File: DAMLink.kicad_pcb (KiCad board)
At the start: 2 copper layers, 41 x 33 mm, 71 parts, among them J1 USB_C_Receptacle_Host, J3 ARM_JTAG_SWD_10_Male, J4 VCCIO_EXT, J5 PicoBlade, P1 USB_C_Plug, SW1 SW_DIP_x04, U1 FT230XQ, U2 PI5A3157CEX, U3 PI5A3157CEX, U4 USB3740B-AI2, U5 SiP32432DR3

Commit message: Add new footprint
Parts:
- removed C6: 100nF, Capacitor_SMD:C_0603_1608Metric
- removed R15: 680R, Resistor_SMD:R_0603_1608Metric
- removed SWD1: TC2030, Connector:Tag-Connect_TC2030-IDC-FP_2x03_P1.27mm_Vertical
- removed TP18: TestPoint_Small, tuna-f1sh/jbr-kicad/Misc.pretty:TestPoint_Pad_D1.0mm_Tight
- added C3: 100nF, Capacitor_SMD:C_0603_1608Metric, F.Cu at (116.5, 45.5)
- added C5: 100nF, Capacitor_SMD:C_0603_1608Metric, F.Cu at (116.5, 48.0)
- added D1: TXD, LED_SMD:LED_0603_1608Metric, F.Cu at (135.9, 45.5)
- added D2: RXD, LED_SMD:LED_0603_1608Metric, F.Cu at (135.9, 48.1)
- added J1: PicoBlade, Connector_Molex:Molex_PicoBlade_53048-0610_1x06_P1.25mm_Horizontal, F.Cu at (155.9, 76.3)
- added J3: PicoBlade, Connector_PinHeader_1.27mm:PinHeader_1x04_P1.27mm_Vertical, F.Cu at (137.0, 54.6)
- added J6: Conn_ST_STDC14, Connector_STDC14:SAMTEC_FTSH-107-01-L-DV-K-A, F.Cu at (171.5, 66.5)
- added JP1: SolderJumper_2_Bridged, Jumper:SolderJumper-2_P1.3mm_Bridged_RoundedPad1.0x1.5mm, F.Cu at (112.3, 46.0)
- added JP5: SolderJumper_3_Bridged12, Jumper:SolderJumper-3_P1.3mm_Bridged12_RoundedPad1.0x1.5mm, F.Cu at (125.7, 67.8)
- added JP6: SolderJumper_2_Bridged, Jumper:SolderJumper-2_P1.3mm_Bridged_RoundedPad1.0x1.5mm, F.Cu at (112.3, 49.6)
- added JP7: SolderJumper_2_Bridged, Jumper:SolderJumper-2_P1.3mm_Bridged_RoundedPad1.0x1.5mm, F.Cu at (112.3, 53.1)
- added JP8: SolderJumper_2_Bridged, Jumper:SolderJumper-2_P1.3mm_Bridged_RoundedPad1.0x1.5mm, F.Cu at (112.3, 56.7)
- added JP9: SolderJumper_2_Bridged, Jumper:SolderJumper-2_P1.3mm_Bridged_RoundedPad1.0x1.5mm, F.Cu at (112.3, 60.2)
- added R10: 680R, Resistor_SMD:R_0603_1608Metric, F.Cu at (120.5, 55.5)
- added R3: 22k, Resistor_SMD:R_0603_1608Metric, F.Cu at (116.5, 50.5)
- added R4: 22k, Resistor_SMD:R_0603_1608Metric, F.Cu at (116.5, 53.0)
- added R5: 1k, Resistor_SMD:R_0603_1608Metric, F.Cu at (116.5, 55.5)
- added R6: 1k, Resistor_SMD:R_0603_1608Metric, F.Cu at (120.5, 45.5)
- added R7: 680R, Resistor_SMD:R_0603_1608Metric, F.Cu at (120.5, 48.0)
- added R8: 680R, Resistor_SMD:R_0603_1608Metric, F.Cu at (120.5, 50.5)
- added R9: 680R, Resistor_SMD:R_0603_1608Metric, F.Cu at (120.5, 53.0)
- added TP1: TestPoint_Small, TestPoint:TestPoint_Pad_D1.0mm, F.Cu at (201.0, 39.9)
- added TP10: TestPoint_Small, TestPoint:TestPoint_Pad_D1.0mm, F.Cu at (201.0, 49.0)
- added TP2: TestPoint_Small, TestPoint:TestPoint_Pad_D1.0mm, F.Cu at (201.0, 42.9)
- added TP9: TestPoint_Small, TestPoint:TestPoint_Pad_D1.0mm, F.Cu at (201.0, 46.0)
- added U2: USB3740B-AI2, Package_DFN_QFN:UQFN-10_1.3x1.8mm_P0.4mm, F.Cu at (136.2, 70.3)
- added U3: TMUX1574RSVR, TMUX1574RSVR:IC_TMUX1574RSVR, F.Cu at (139.2, 78.8)
- added U4: USBLC6-4SC6, Package_TO_SOT_SMD:SOT-23-6, F.Cu at (134.4, 37.2)
- added U6: USBLC6-4SC6, Package_TO_SOT_SMD:SOT-23-6, F.Cu at (134.4, 41.9)
- C1: value 100nF -> 10nF
- J3: value ARM_JTAG_SWD_10_Male -> PicoBlade; footprint tuna-f1sh/jbr-kicad/Misc.pretty:20021521-00010T1LF -> Connector_PinHeader_1.27mm:PinHeader_1x04_P1.27mm_Vertical
- J5: value PicoBlade -> TC2050-IDC; footprint Connector_PinHeader_1.27mm:PinHeader_1x04_P1.27mm_Vertical -> TC2050-IDC:TAG-CONNECT_TC2050-IDC
- JP2: value SolderJumper_2_Bridged -> SolderJumper_3_Bridged12; footprint Jumper:SolderJumper-2_P1.3mm_Bridged_RoundedPad1.0x1.5mm -> Jumper:SolderJumper-3_P1.3mm_Bridged12_RoundedPad1.0x1.5mm
- R1, R2: value 1k -> 5k1
- R5, R6: value 22k -> 1k
- TP11, TP12, TP13, TP14, TP15, TP16, TP17, TP3, TP4, TP5, TP6, TP7, TP8: footprint tuna-f1sh/jbr-kicad/Misc.pretty:TestPoint_Pad_D1.0mm_Tight -> TestPoint:TestPoint_Pad_D1.0mm
- TP13: renamed from TP9; footprint tuna-f1sh/jbr-kicad/Misc.pretty:TestPoint_Pad_D1.0mm_Tight -> TestPoint:TestPoint_Pad_D1.0mm
- TP14: renamed from TP2; footprint tuna-f1sh/jbr-kicad/Misc.pretty:TestPoint_Pad_D1.0mm_Tight -> TestPoint:TestPoint_Pad_D1.0mm
- TP15: renamed from TP19; footprint tuna-f1sh/jbr-kicad/Misc.pretty:TestPoint_Pad_D1.0mm_Tight -> TestPoint:TestPoint_Pad_D1.0mm
- TP16: renamed from TP10; footprint tuna-f1sh/jbr-kicad/Misc.pretty:TestPoint_Pad_D1.0mm_Tight -> TestPoint:TestPoint_Pad_D1.0mm
- TP17: renamed from TP1; footprint tuna-f1sh/jbr-kicad/Misc.pretty:TestPoint_Pad_D1.0mm_Tight -> TestPoint:TestPoint_Pad_D1.0mm
- U2: value PI5A3157CEX -> USB3740B-AI2; footprint Package_TO_SOT_SMD:SOT-363_SC-70-6 -> Package_DFN_QFN:UQFN-10_1.3x1.8mm_P0.4mm
- U3: value PI5A3157CEX -> TMUX1574RSVR; footprint Package_TO_SOT_SMD:SOT-363_SC-70-6 -> TMUX1574RSVR:IC_TMUX1574RSVR
- U4: value USB3740B-AI2 -> USBLC6-4SC6; footprint Package_DFN_QFN:UQFN-10_1.3x1.8mm_P0.4mm -> Package_TO_SOT_SMD:SOT-23-6
- moved G*** 50.6 mm to (214.1, 64.6)
- moved J5 33.4 mm to (181.5, 60.5), turned to 180 degrees
- moved J3 26.2 mm to (155.6, 39.5), turned to 90 degrees
- moved U3 1.30 mm to (173.0, 54.5)
- moved TP4 0.75 mm to (168.0, 50.5)
- renumbered C2 to C1, C3 to C2, D4 to D3, J1 to J2, JP5 to JP2, JP6 to JP3, R12 to R1, R14 to R11, R16 to R12, R10 to R13, R11 to R14, R13 to R2
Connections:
- C1 pad 1: +3V3 -> Net-(C1-Pad1)
- C1 pad 1: Net-(C2-Pad1) -> Net-(C1-Pad1)
- FB1 pad 1: Net-(C2-Pad1) -> Net-(C1-Pad1)
- J2 pad A4: Net-(C2-Pad1) -> Net-(C1-Pad1)
- J2 pad A9: Net-(C2-Pad1) -> Net-(C1-Pad1)
- J2 pad B4: Net-(C2-Pad1) -> Net-(C1-Pad1)
- J2 pad B9: Net-(C2-Pad1) -> Net-(C1-Pad1)
- J3 pad 1: /VREF -> VCC
- J3 pad 2: /SWDIO -> /DEV_TXD
- J3 pad 3: GND -> /DEV_RXD
- J3 pad 4: /SWCLK -> GND
- J5 pad 1: VCC -> /VREF
- J5 pad 2: /DEV_TXD -> /SWDIO
- J5 pad 3: /DEV_RXD -> GND
- J5 pad 4: GND -> /SWCLK
- JP1 pad 1: /DEV_RXD -> Net-(JP1-A)
- JP1 pad 2: Net-(JP1-B) -> VBUS
- JP2 pad 3: Net-(JP5-B) -> Net-(JP2-B)
- JP2 pad 1: /DEV_TXD -> /VTARGET
- JP2 pad 2: Net-(JP2-B) -> VCC
- JP3 pad 1: /VTARGET -> +3V3
- JP3 pad 2: /VREF -> Net-(JP2-B)
- JP3 pad 3: VCC -> Net-(J4-Pin_1)
- JP3 pad 2: Net-(JP5-B) -> Net-(JP2-B)
- JP7 pad 1: Net-(JP7-A) -> /DEV_TXD
- JP7 pad 2: VBUS -> Net-(J6-VCP_TX)
- P1 pad A2: /SWDIO -> /DEV_TX+
- P1 pad A3: /SWCLK -> /DEV_TX-
- P1 pad B2: /SWDIO -> /DEV_TX+
- P1 pad B3: /SWCLK -> /DEV_TX-
- R1 pad 1: Net-(D1-K) -> /HOST_CC2
- R1 pad 2: /TXLED/CB1 -> GND
- R2 pad 1: Net-(D2-K) -> /HOST_CC1
- R2 pad 2: /RXLED/CB2 -> GND
- R3 pad 1: /UART_USB -> /~{PASS_USB}
- R4 pad 1: /~{PASS_USB} -> /UART_USB
- R5 pad 1: /SWT_RX+ -> Net-(D1-K)
- R5 pad 2: GND -> /TXLED/CB1
- R6 pad 1: /SWT_RX- -> Net-(D2-K)
- R6 pad 2: GND -> /RXLED/CB2
- TP11 pad 1: /HOST_D+ -> /DEV_D+
- TP12 pad 1: /HOST_D- -> /DEV_D-
- TP13 pad 1: /UART_D+ -> /SWDIO
- TP14 pad 1: /UART_D- -> /SWCLK
- TP15 pad 1: /DEV_D+ -> /VREF
- TP16 pad 1: /DEV_D- -> /~{RESET}
- TP17 pad 1: /DEV_RX+ -> /SWO
- TP3 pad 1: /TXDEN/CB0 -> /~{PASS_USB}
- TP4 pad 1: /TXLED/CB1 -> /UART_USB
- TP5 pad 1: /RXLED/CB2 -> /TXDEN/CB0
- TP6 pad 1: /SLEEP/CB3 -> /TXLED/CB1
- TP7 pad 1: /~{PASS_USB} -> /RXLED/CB2
- TP8 pad 1: /UART_USB -> /SLEEP/CB3
- U1 pad 10: Net-(JP7-A) -> Net-(JP1-A)
- U1 pad 15: /DEV_TXD -> Net-(JP8-A)
- U1 pad 2: /DEV_RXD -> Net-(JP9-A)
- U2 pad 1: Net-(JP1-B) -> /DEV_D-
- U2 pad 2: GND -> /DEV_D+
- U2 pad 3: /~{RESET} -> /~{PASS_USB}
- U2 pad 4: /DEV_RX- -> /UART_USB
- U2 pad 5: VCC -> VBUS
- U2 pad 6: /SWT_RX- -> /UART_D+
- U3 pad 1: Net-(JP2-B) -> /IO0
- U3 pad 2: GND -> /DEV_TX-
- U3 pad 3: /SWO -> /SWDIO
- U3 pad 4: /DEV_RX+ -> /IO1
- U3 pad 5: VCC -> /DEV_TX+
- U3 pad 6: /SWT_RX+ -> GND
- U4 pad 1: /DEV_D- -> /DEV_RX-
- U4 pad 2: /DEV_D+ -> GND
- U4 pad 3: /~{PASS_USB} -> /DEV_RX+
- U4 pad 4: /UART_USB -> /VTARGET
- U4 pad 6: /UART_D+ -> /VTARGET
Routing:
- net /~{RESET}: track 59.6 -> 0.00 mm, vias 5 -> 0
- net VCC: track 87.4 -> 34.9 mm, vias 6 -> 1
- net /SWT_RX+: track 51.7 -> 0.00 mm, vias 6 -> 0
- net /RXLED/CB2: track 46.5 -> 0.00 mm, vias 3 -> 0
- net /SWCLK: track 44.3 -> 0.00 mm, vias 4 -> 0
- net /SWDIO: track 44.0 -> 0.00 mm, vias 4 -> 0
- net /DEV_D-: track 29.4 -> 0.00 mm, vias 2 -> 0
- net /SWO: track 28.1 -> 0.00 mm, vias 4 -> 0
- net /DEV_D+: track 28.1 -> 0.00 mm, vias 2 -> 0
- net GND: track 58.8 -> 31.8 mm, vias 5 -> 4
- net /~{DEV_ON}: track 26.0 -> 1.54 mm, vias 4 -> 0
- net /VTARGET: track 38.1 -> 13.7 mm, vias 6 -> 2
- net /UART_USB: track 22.6 -> 0.00 mm, vias 3 -> 0
- net /DEV_RX+: track 33.4 -> 12.2 mm, vias 3 -> 0
- net /DEV_RX-: track 29.8 -> 8.98 mm, vias 3 -> 0
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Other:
- board text added: "DAMLink R${REVISION}"
- board text removed: "Minnow R${REVISION}"

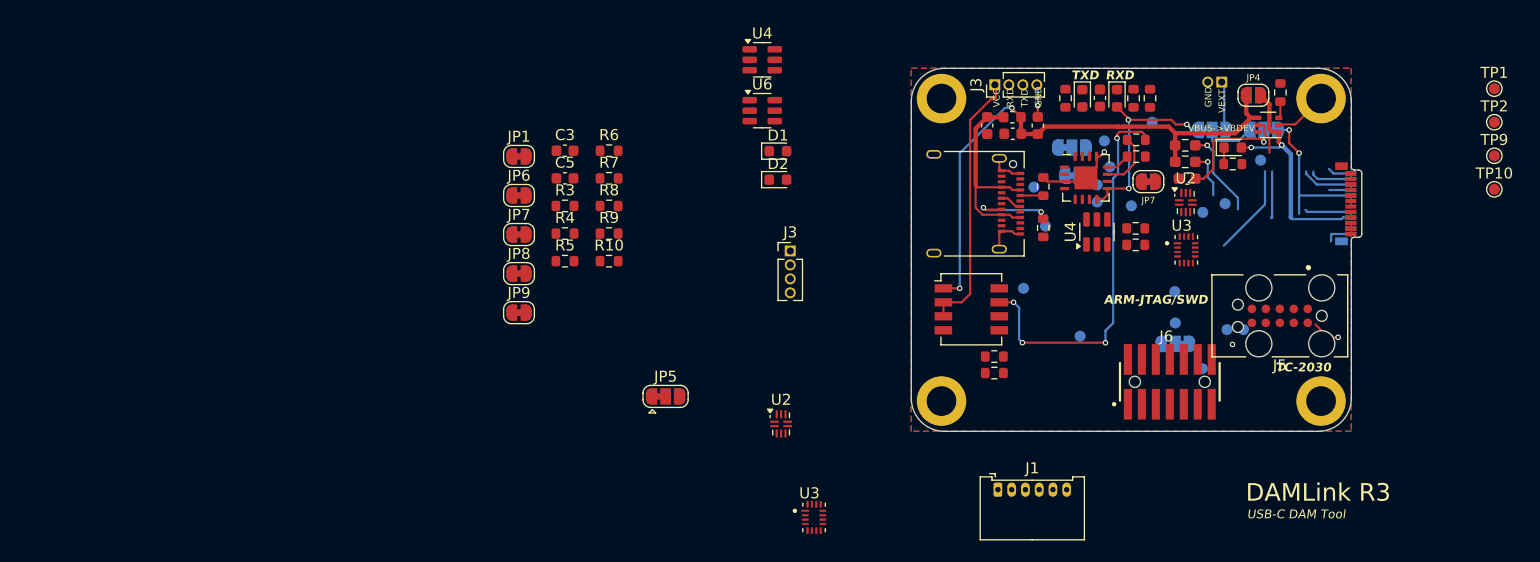
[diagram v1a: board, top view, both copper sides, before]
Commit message: Remove wrong libraries
Remove "altium" libraries which where downloaded wrong from SnapEDA.

Import correct libraries from Manufracturer and from UltranLibrary

Clear whole PCB.
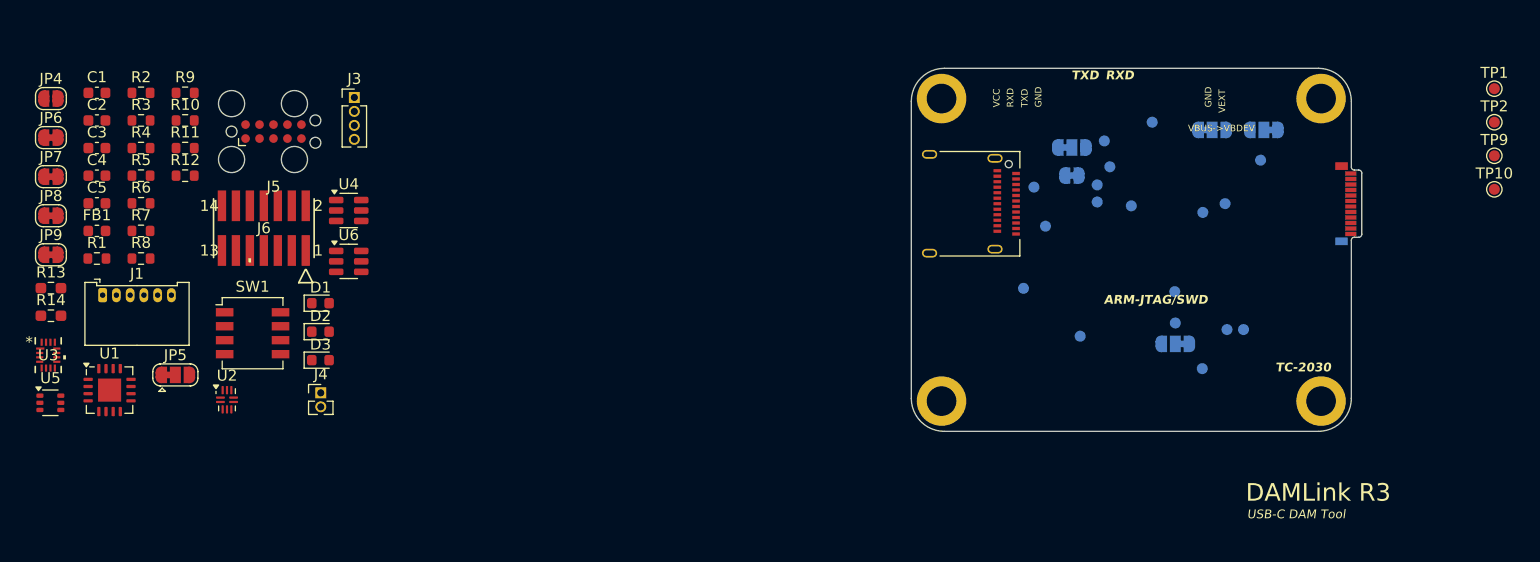
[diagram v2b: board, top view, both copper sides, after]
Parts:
- removed the C1 at (165.2, 40.7)
- removed the C1 at (154.9, 43.2)
- removed the C5 at (173.1, 48.0)
- removed the C5 at (116.5, 48.0)
- removed the D1 at (135.9, 45.5)
- removed the D1 at (163.6, 40.7)
- removed the D2 at (166.7, 40.7)
- removed the D2 at (135.9, 48.1)
- removed the J3 at (137.0, 54.6)
- removed the J3 at (155.6, 39.5)
- removed the JP1 at (112.3, 46.0)
- removed the JP7 at (112.3, 53.1)
- removed the JP7 at (169.6, 48.3)
- removed the R1 at (160.0, 52.5)
- removed the R1 at (162.0, 40.7)
- removed the R2 at (168.2, 40.7)
- removed the R2 at (160.0, 48.8)
- removed the R3 at (116.5, 50.5)
- removed the R3 at (168.4, 52.5)
- removed the R4 at (116.5, 53.0)
- removed the R4 at (168.4, 54.0)
- removed the R5 at (116.5, 55.5)
- removed the R5 at (155.6, 65.7)
- removed the R6 at (120.5, 45.5)
- removed the R6 at (155.6, 64.2)
- removed the R7 at (120.5, 48.0)
- removed the R7 at (168.4, 46.0)
- removed the R8 at (120.5, 50.5)
- removed the R8 at (168.4, 44.5)
- removed the R9 at (169.7, 40.7)
- removed the R9 at (120.5, 53.0)
- removed the U2 at (136.2, 70.3)
- removed the U2 at (172.9, 50.2)
- removed the U3 at (139.2, 78.8)
- removed the U3 at (173.0, 54.5)
- removed the U4 at (134.4, 37.2)
- removed the U4 at (164.9, 52.9)
- added C1: 10nF, Capacitor_SMD:C_0603_1608Metric, F.Cu at (74.0, 40.2)
- added C5: 100nF, Capacitor_SMD:C_0603_1608Metric, F.Cu at (74.0, 50.3)
- added D1: TXD, LED_SMD:LED_0603_1608Metric, F.Cu at (94.3, 59.4)
- added D2: RXD, LED_SMD:LED_0603_1608Metric, F.Cu at (94.3, 61.9)
- added J3: PicoBlade, Connector_PinHeader_1.27mm:PinHeader_1x04_P1.27mm_Vertical, F.Cu at (97.4, 40.6)
- added JP7: SolderJumper_2_Bridged, Jumper:SolderJumper-2_P1.3mm_Bridged_RoundedPad1.0x1.5mm, F.Cu at (69.8, 47.9)
- added R1: 5k1, Resistor_SMD:R_0603_1608Metric, F.Cu at (74.0, 55.3)
- added R2: 5k1, Resistor_SMD:R_0603_1608Metric, F.Cu at (78.0, 40.2)
- added R3: 22k, Resistor_SMD:R_0603_1608Metric, F.Cu at (78.0, 42.7)
- added R4: 22k, Resistor_SMD:R_0603_1608Metric, F.Cu at (78.0, 45.2)
- added R5: 1k, Resistor_SMD:R_0603_1608Metric, F.Cu at (78.0, 47.8)
- added R6: 1k, Resistor_SMD:R_0603_1608Metric, F.Cu at (78.0, 50.3)
- added R7: 680R, Resistor_SMD:R_0603_1608Metric, F.Cu at (78.0, 52.8)
- added R8: 680R, Resistor_SMD:R_0603_1608Metric, F.Cu at (78.0, 55.3)
- added R9: 680R, Resistor_SMD:R_0603_1608Metric, F.Cu at (82.0, 40.2)
- added U2: USB3740B-AI2, Package_DFN_QFN:UQFN-10_1.3x1.8mm_P0.4mm, F.Cu at (85.8, 68.1)
- added U3: TMUX1574RSVR, TMUX1574RSVR:RSV16_TEX, F.Cu at (69.5, 64.1)
- added U4: USBLC6-4SC6, Package_TO_SOT_SMD:SOT-23-6, F.Cu at (96.9, 50.9)
- J5: footprint TC2050-IDC:TAG-CONNECT_TC2050-IDC -> Connector:Tag-Connect_TC2050-IDC-FP_2x05_P1.27mm_Vertical
- J6: footprint Connector_STDC14:SAMTEC_FTSH-107-01-L-DV-K-A -> Connector_STDC14:CON14_2X7_DUK_FTSH_SAI
- moved U5 113.6 mm to (69.7, 68.4), turned to 0 degrees
- moved JP4 109.3 mm to (69.8, 40.8)
- moved R14 104.3 mm to (69.8, 60.5)
- moved R13 103.7 mm to (69.8, 58.0)
- moved R11 99.7 mm to (82.0, 45.2), turned to 0 degrees
- moved R12 95.2 mm to (82.0, 47.8)
- moved J5 93.0 mm to (90.0, 43.8), turned to 0 degrees
- moved U1 90.8 mm to (75.1, 67.2)
- moved J4 86.6 mm to (94.3, 67.5), turned to 0 degrees
- moved C2 85.5 mm to (74.0, 42.7), turned to 0 degrees
- moved D3 85.1 mm to (94.3, 64.5)
- moved FB1 83.9 mm to (74.0, 52.8)
- moved J6 83.5 mm to (89.1, 52.5)
- moved C4 83.3 mm to (74.0, 47.8), turned to 0 degrees
- moved J1 83.3 mm to (74.5, 58.6)
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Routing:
- net VBUS: track 51.8 -> 0.00 mm, vias 2 -> 0
- net /SWT_RX-: track 35.5 -> 0.00 mm, vias 4 -> 0
- net VCC: track 34.9 -> 0.00 mm, vias 1 -> 0
- net GND: track 31.8 -> 0.00 mm, vias 4 -> 0
- net /VBUS_DEV: track 23.9 -> 0.00 mm, vias 2 -> 0
- net Net-(C1-Pad1): track 18.8 -> 0.00 mm
- net +3V3: track 18.1 -> 0.00 mm, vias 3 -> 0
- net /VTARGET: track 13.7 -> 0.00 mm, vias 2 -> 0
- net /DEV_CC2: track 12.3 -> 0.00 mm, vias 1 -> 0
- net /DEV_RX+: track 12.2 -> 0.00 mm
- net /DEV_RX-: track 8.98 -> 0.00 mm
- net /HOST_CC2: track 7.51 -> 0.00 mm, vias 2 -> 0
- net /TXLED/CB1: track 5.36 -> 0.00 mm
- net Net-(JP2-B): track 4.78 -> 0.00 mm
- net /DEV_CC1: track 4.39 -> 0.00 mm, vias 1 -> 0
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- removed copper zone on B.Cu, net GND
- removed copper zone on F.Cu, net GND

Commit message: Update DAMLink.kicad_pcb
Remove Logo from
Add information in header
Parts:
- removed the G*** at (179.5, 68.0)
- removed the G*** at (168.0, 68.0)
